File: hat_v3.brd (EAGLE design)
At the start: 65 x 56.5 mm, 41 parts, among them U1 ADS1115IDGST, U2 ADXL345, U3 MCP2515-I/SO, U4 MCP2551, X1 16Mhz

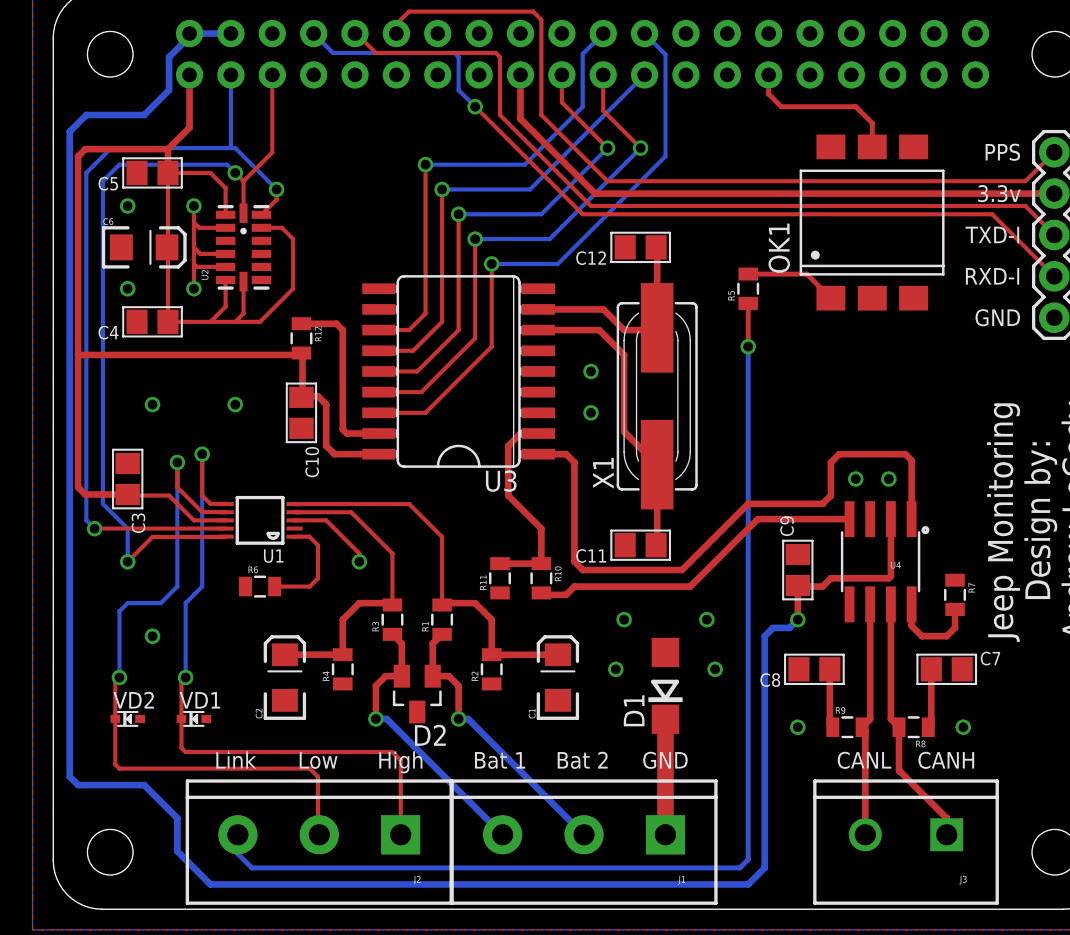
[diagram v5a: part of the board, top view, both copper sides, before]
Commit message: Minor tweaks to GND plane
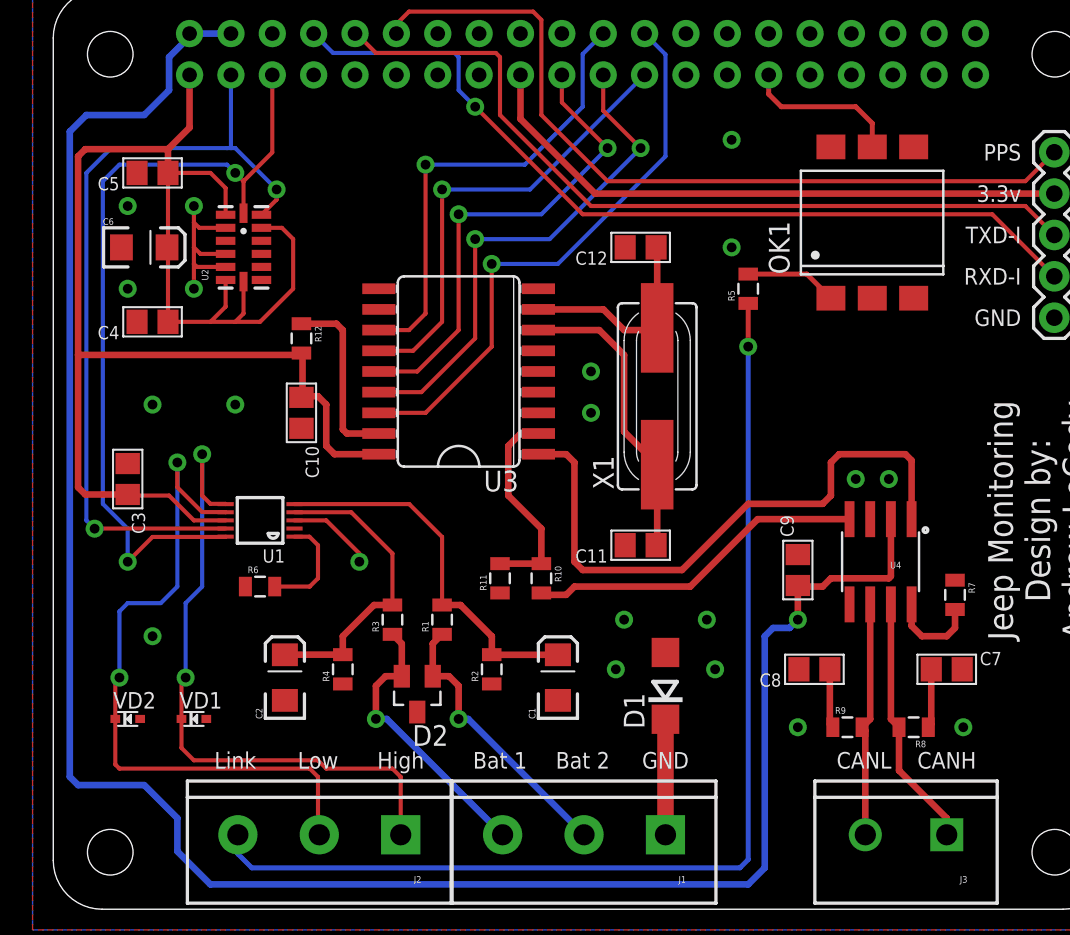
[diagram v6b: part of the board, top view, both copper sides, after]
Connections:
- net N$1 renamed VEHICLE-GND
- net N$5 renamed RS
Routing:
- net BAT-2: track 19.5 -> 18.8 mm
- net BAT-1: track 23.8 -> 23.1 mm
- net SHUNT-HIGH-INPUT: track 41.1 -> 40.5 mm
- net GND: vias 18 -> 20
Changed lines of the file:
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@@
 </class>
 </classes>
-<designrules name="oshpark-2layer">
-<description language="de">&lt;b&gt;EAGLE Design Rules&lt;/b&gt;
+<designrules name="SparkFun">
+<description language="en">&lt;b&gt;EAGLE Design Rules&lt;/b&gt;
 &lt;p&gt;
-Die Standard-Design-Rules sind so gewählt, dass sie für
-die meisten Anwendungen passen. Sollte ihre Platine
-besondere Anforderungen haben, treffen Sie die erforderlichen
-Einstellungen hier und speichern die Design Rules unter
-einem neuen Namen ab.</description>
-<description language="en">&lt;b&gt;Laen's PCB Order Design Rules&lt;/b&gt;
-&lt;p&gt;
-Please make sure your boards conform to these design rules.</description>
+The default Design Rules have been set to cover
+a wide range of applications. Your particular design
+may have different requirements, so please make the
+necessary adjustments and save your customized
+design rules under a new name.</description>
 <param name="layerSetup" value="(1*16)"/>
-<param name="mtCopper" value="0.0356mm 0.0356mm 0.0356mm 0.0356mm 0.0356mm 0.0356mm 0.0356mm 0.0356mm 0.0356mm 0.0356mm 0.0356mm 0.0356mm 0.0356mm 0.0356mm 0.0356mm 0.0356mm"/>
-<param name="mtIsolate" value="1.5011mm 0.1499mm 0.2007mm 0.1499mm 0.2007mm 0.1499mm 0.2007mm 0.1499mm 0.2007mm 0.1499mm 0.2007mm 0.1499mm 0.2007mm 0.1499mm 0.2007mm"/>
-<param name="mdWireWire" value="6mil"/>
-<param name="mdWirePad" value="6mil"/>
-<param name="mdWireVia" value="6mil"/>
-<param name="mdPadPad" value="6mil"/>
-<param name="mdPadVia" value="6mil"/>
-<param name="mdViaVia" value="6mil"/>
-<param name="mdSmdPad" value="6mil"/>
-<param name="mdSmdVia" value="6mil"/>
-<param name="mdSmdSmd" value="6mil"/>
+<param name="mtCopper" value="0.035mm 0.035mm 0.035mm 0.035mm 0.035mm 0.035mm 0.035mm 0.035mm 0.035mm 0.035mm 0.035mm 0.035mm 0.035mm 0.035mm 0.035mm 0.035mm"/>
+<param name="mtIsolate" value="1.5mm 0.15mm 0.2mm 0.15mm 0.2mm 0.15mm 0.2mm 0.15mm 0.2mm 0.15mm 0.2mm 0.15mm 0.2mm 0.15mm 0.2mm"/>
+<param name="mdWireWire" value="8mil"/>
+<param name="mdWirePad" value="8mil"/>
+<param name="mdWireVia" value="8mil"/>
+<param name="mdPadPad" value="8mil"/>
+<param name="mdPadVia" value="8mil"/>
+<param name="mdViaVia" value="8mil"/>
+<param name="mdSmdPad" value="8mil"/>
+<param name="mdSmdVia" value="8mil"/>
+<param name="mdSmdSmd" value="8mil"/>
 <param name="mdViaViaSameLayer" value="8mil"/>
 <param name="mnLayersViaInSmd" value="2"/>
-<param name="mdCopperDimension" value="15mil"/>
-<param name="mdDrill" value="6mil"/>
+<param name="mdCopperDimension" value="8mil"/>
+<param name="mdDrill" value="8mil"/>
 <param name="mdSmdStop" value="0mil"/>
-<param name="msWidth" value="6mil"/>
-<param name="msDrill" value="13mil"/>
-<param name="msMicroVia" value="13mil"/>
+<param name="msWidth" value="8mil"/>
+<param name="msDrill" value="20mil"/>
+<param name="msMicroVia" value="9.99mm"/>
 <param name="msBlindViaRatio" value="0.5"/>
 <param name="rvPadTop" value="0.25"/>
@@
 <param name="rvMicroViaOuter" value="0.25"/>
 <param name="rvMicroViaInner" value="0.25"/>
-<param name="rlMinPadTop" value="7mil"/>
+<param name="rlMinPadTop" value="12mil"/>
 <param name="rlMaxPadTop" value="20mil"/>
-<param name="rlMinPadInner" value="7mil"/>
+<param name="rlMinPadInner" value="10mil"/>
 <param name="rlMaxPadInner" value="20mil"/>
-<param name="rlMinPadBottom" value="7mil"/>
+<param name="rlMinPadBottom" value="12mil"/>
 <param name="rlMaxPadBottom" value="20mil"/>
-<param name="rlMinViaOuter" value="7mil"/>
+<param name="rlMinViaOuter" value="10mil"/>
 <param name="rlMaxViaOuter" value="20mil"/>
-<param name="rlMinViaInner" value="7mil"/>
+<param name="rlMinViaInner" value="10mil"/>
 <param name="rlMaxViaInner" value="20mil"/>
 <param name="rlMinMicroViaOuter" value="4mil"/>
@@
 <param name="mvStopFrame" value="1"/>
 <param name="mvCreamFrame" value="0"/>
-<param name="mlMinStopFrame" value="2.5mil"/>
-<param name="mlMaxStopFrame" value="2.5mil"/>
+<param name="mlMinStopFrame" value="4mil"/>
+<param name="mlMaxStopFrame" value="4mil"/>
 <param name="mlMinCreamFrame" value="0mil"/>
 <param name="mlMaxCreamFrame" value="0mil"/>
-<param name="mlViaStopLimit" value="0mil"/>
+<param name="mlViaStopLimit" value="20mil"/>
 <param name="srRoundness" value="0"/>
 <param name="srMinRoundness" value="0mil"/>
@@
 <via x="55.88" y="11.176" extent="1-16" drill="0.6" shape="square"/>
 <via x="40.64" y="14.732" extent="1-16" drill="0.6" shape="square"/>
+<via x="41.656" y="40.64" extent="1-16" drill="0.6" shape="square"/>
+<via x="41.656" y="47.244" extent="1-16" drill="0.6" shape="square"/>
 </signal>
 <signal name="TXD">
@@
 <wire x1="21.86" y1="24.876" x2="23.876" y2="22.86" width="0.254" layer="1"/>
 <wire x1="23.876" y1="22.86" x2="23.876" y2="18.68" width="0.254" layer="1"/>
-<wire x1="26.924" y1="15.632" x2="26.924" y2="17.78" width="0.4064" layer="1"/>
-<wire x1="26.924" y1="17.78" x2="25.908" y2="18.796" width="0.4064" layer="1"/>
-<wire x1="25.908" y1="18.796" x2="23.992" y2="18.796" width="0.4064" layer="1"/>
-<wire x1="23.992" y1="18.796" x2="23.876" y2="18.68" width="0.4064" layer="1"/>
 <wire x1="30.988" y1="15.624" x2="26.932" y2="15.624" width="0.4064" layer="1"/>
 <wire x1="26.932" y1="15.624" x2="26.924" y2="15.632" width="0.4064" layer="1"/>
+<wire x1="26.932" y1="15.624" x2="26.932" y2="16.756" width="0.4064" layer="1"/>
+<wire x1="26.932" y1="16.756" x2="25.008" y2="18.68" width="0.4064" layer="1"/>
+<wire x1="25.008" y1="18.68" x2="23.876" y2="18.68" width="0.4064" layer="1"/>
 </signal>
 <signal name="BAT-2">
@@
 <wire x1="14.224" y1="15.624" x2="14.232" y2="15.632" width="0.4064" layer="1"/>
 <wire x1="14.232" y1="15.632" x2="17.78" y2="15.632" width="0.4064" layer="1"/>
-<wire x1="17.78" y1="15.632" x2="17.78" y2="17.78" width="0.4064" layer="1"/>
-<wire x1="17.78" y1="17.78" x2="18.796" y2="18.796" width="0.4064" layer="1"/>
-<wire x1="18.796" y1="18.796" x2="20.712" y2="18.796" width="0.4064" layer="1"/>
-<wire x1="20.712" y1="18.796" x2="20.828" y2="18.68" width="0.4064" layer="1"/>
+<wire x1="17.78" y1="15.632" x2="17.78" y2="16.764" width="0.4064" layer="1"/>
+<wire x1="17.78" y1="16.764" x2="19.696" y2="18.68" width="0.4064" layer="1"/>
+<wire x1="19.696" y1="18.68" x2="20.828" y2="18.68" width="0.4064" layer="1"/>
 </signal>
 <signal name="ADDR">
@@
 <contactref element="U1" pad="6"/>
 <contactref element="VD1" pad="C"/>
-<wire x1="7.874" y1="11.684" x2="7.874" y2="9.906" width="0.254" layer="1"/>
-<wire x1="7.874" y1="9.906" x2="8.128" y2="9.652" width="0.254" layer="1"/>
-<wire x1="8.128" y1="9.652" x2="20.828" y2="9.652" width="0.254" layer="1"/>
-<wire x1="20.828" y1="9.652" x2="21.336" y2="9.144" width="0.254" layer="1"/>
-<wire x1="21.336" y1="9.144" x2="21.336" y2="4.572" width="0.254" layer="1"/>
 <wire x1="10.5869" y1="24.876" x2="10.5709" y2="24.892" width="0.254" layer="1"/>
 <wire x1="10.5709" y1="24.892" x2="9.652" y2="24.892" width="0.254" layer="1"/>
@@
 <wire x1="8.128" y1="14.224" x2="7.874" y2="13.97" width="0.254" layer="1"/>
 <wire x1="7.874" y1="13.97" x2="7.874" y2="11.684" width="0.254" layer="1"/>
+<wire x1="7.874" y1="11.684" x2="7.874" y2="9.906" width="0.254" layer="1"/>
+<wire x1="7.874" y1="9.906" x2="8.636" y2="9.144" width="0.254" layer="1"/>
+<wire x1="8.636" y1="9.144" x2="16.256" y2="9.144" width="0.254" layer="1"/>
+<wire x1="16.256" y1="9.144" x2="16.764" y2="8.636" width="0.254" layer="1"/>
+<wire x1="16.764" y1="8.636" x2="20.828" y2="8.636" width="0.254" layer="1"/>
+<wire x1="20.828" y1="8.636" x2="21.336" y2="8.128" width="0.254" layer="1"/>
+<wire x1="21.336" y1="8.128" x2="21.336" y2="4.572" width="0.254" layer="1"/>
 </signal>
 <signal name="SHUNT-LOW-INPUT">
@@
 <wire x1="46.271" y1="39" x2="47.752" y2="37.519" width="0.3048" layer="1"/>
 </signal>
-<signal name="N$1">
+<signal name="VEHICLE-GND">
 <contactref element="J1" pad="1"/>
 <contactref element="D1" pad="C"/>
@@
 <wire x1="30.088" y1="19.304" x2="29.972" y2="19.42" width="0.4064" layer="1"/>
 </signal>
-<signal name="N$5">
+<signal name="RS">
 <contactref element="U4" pad="8"/>
 <contactref element="R7" pad="2"/>

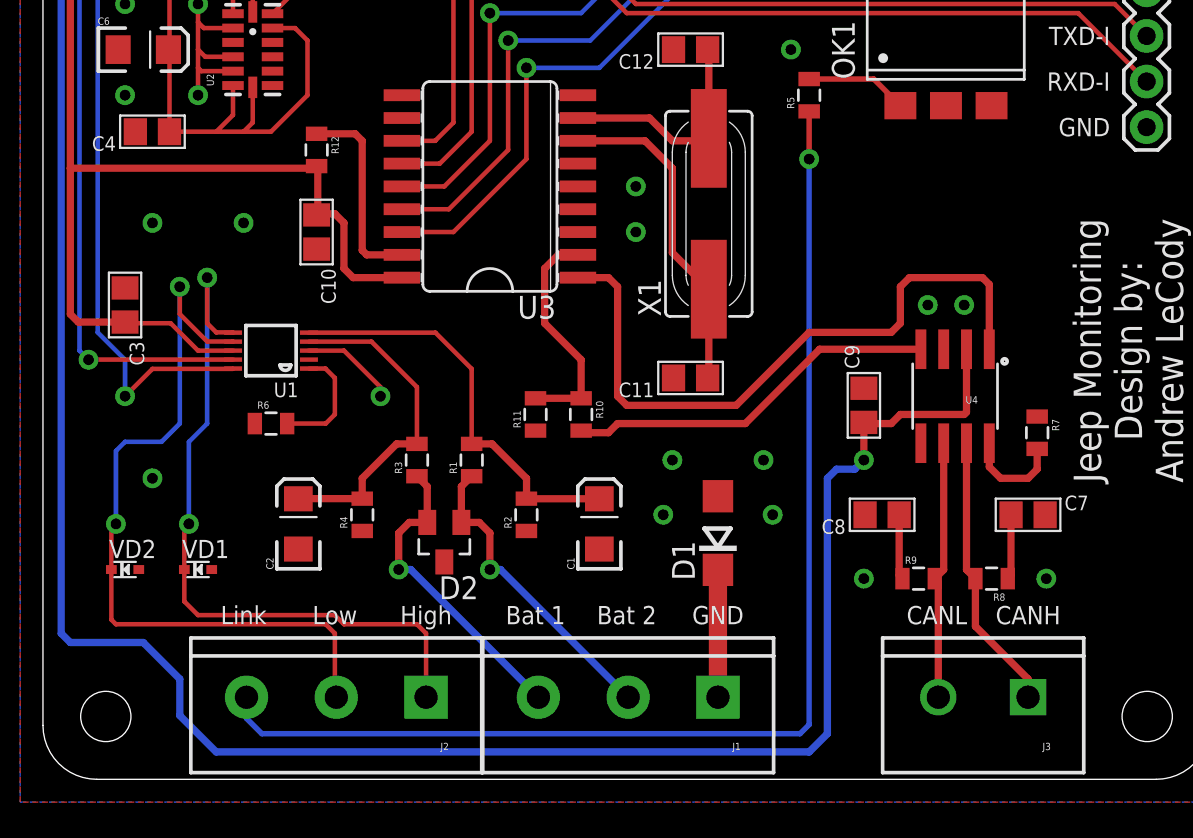
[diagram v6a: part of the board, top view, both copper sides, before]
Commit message: Switched to 3.5mm screw terminals
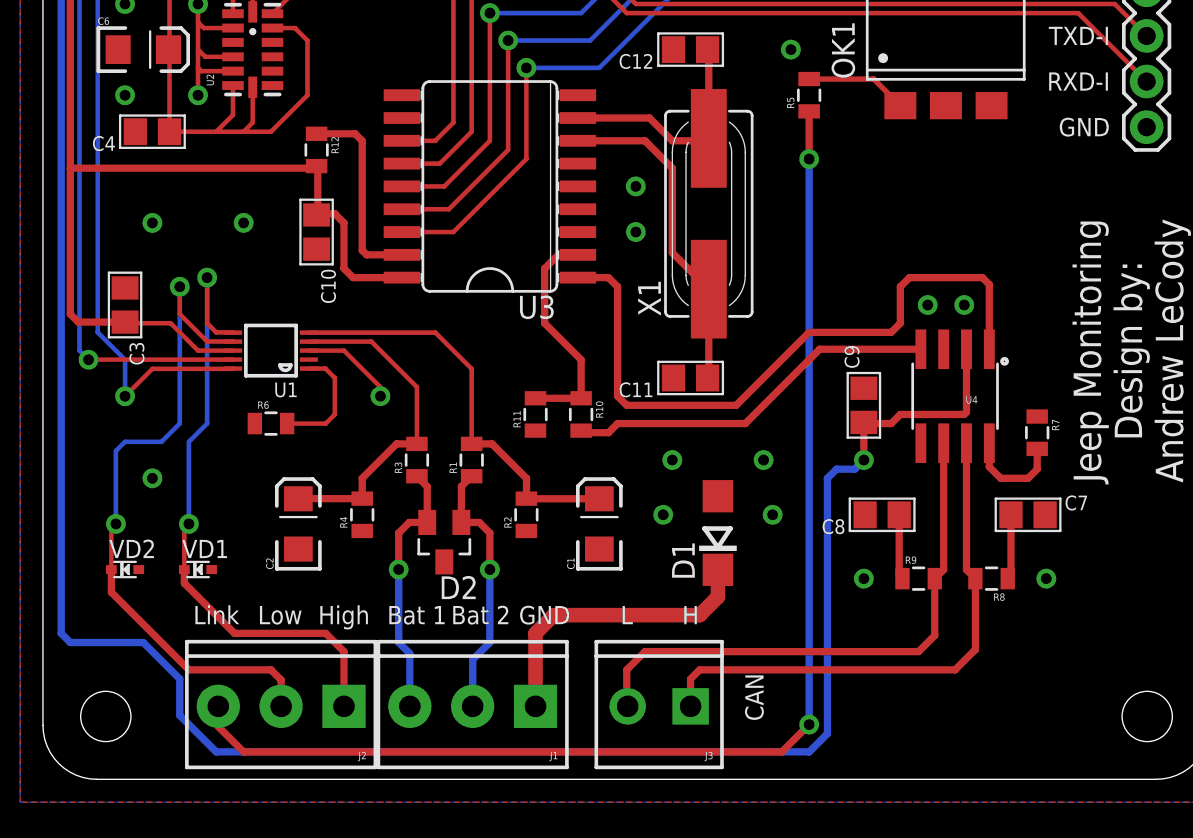
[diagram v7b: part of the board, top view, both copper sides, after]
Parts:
- J1, J2: device SparkFun-Connectors:SCREWTERMINAL-5MM-3 -> SparkFun-Connectors:SCREWTERMINAL-3.5MM-3
- J3: device SparkFun-Connectors:SCREWTERMINAL-5MM-2 -> SparkFun-Connectors:SCREWTERMINAL-3.5MM-2
- moved J3 18.8 mm to (36.1, 4.06)
- moved J1 10.2 mm to (27.4, 4.06)
- moved J2 4.60 mm to (16.8, 4.06)
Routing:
- net CANL: track 14.4 -> 30.9 mm
- net CANH: track 15.6 -> 29.8 mm
- net VEHICLE-GND: track 7.09 -> 16.6 mm
- net SHUNT-HIGH-INPUT: track 40.5 -> 35.3 mm
- net SHUNT-LOW-INPUT: track 42.8 -> 37.9 mm
- net BAT-2-INPUT: track 17.4 -> 14.6 mm
- net BAT-1-INPUT: track 17.3 -> 14.7 mm
- net LINKED-INPUT: track 67.2 -> 69.4 mm, vias 1 -> 2
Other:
- board text added: "CAN"
- board text added: "H"
- board text added: "L"
- board text removed: "CANH"
- board text removed: "CANL"
